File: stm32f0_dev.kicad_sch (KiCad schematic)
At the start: 38 parts, among them J1 USB_C_Receptacle_USB2.0, J2 left_bank, J3 SWD_header, J4 right_bank, SW1 SW_Push_Open_Dual, SW2 SW_SPDT, U2 AP2112K-3.3, U3 SN74LVC2G04DCKR, U4 CH340C, U5 MT29F2G01ABAGDWB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

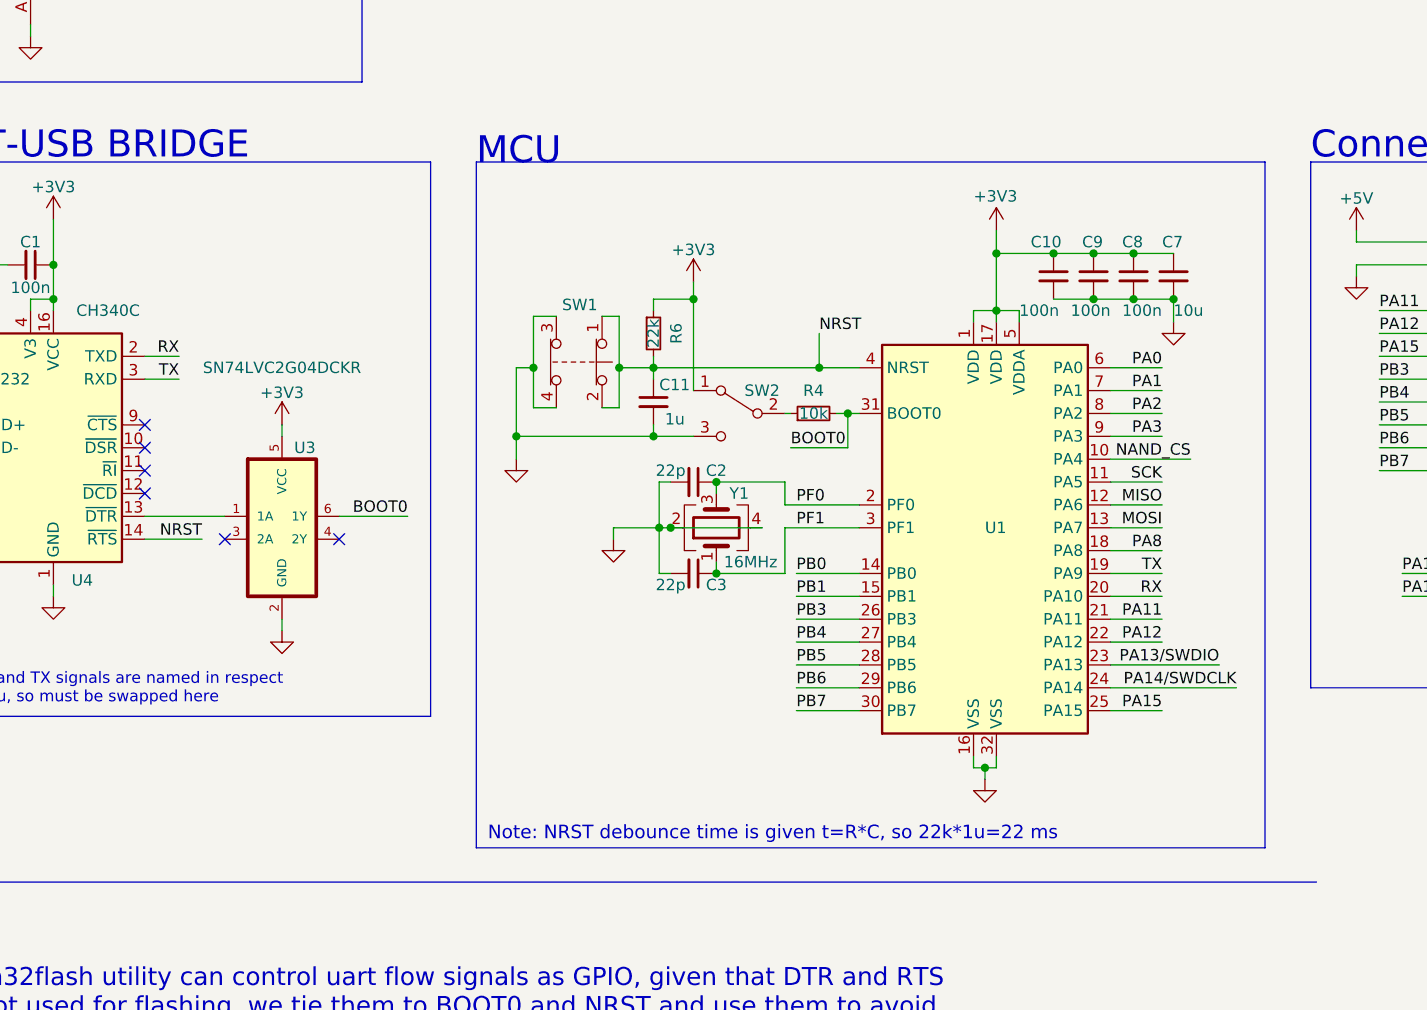
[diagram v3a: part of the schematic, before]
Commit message: Removed useless boot0 switch, uart IC is driving that signal
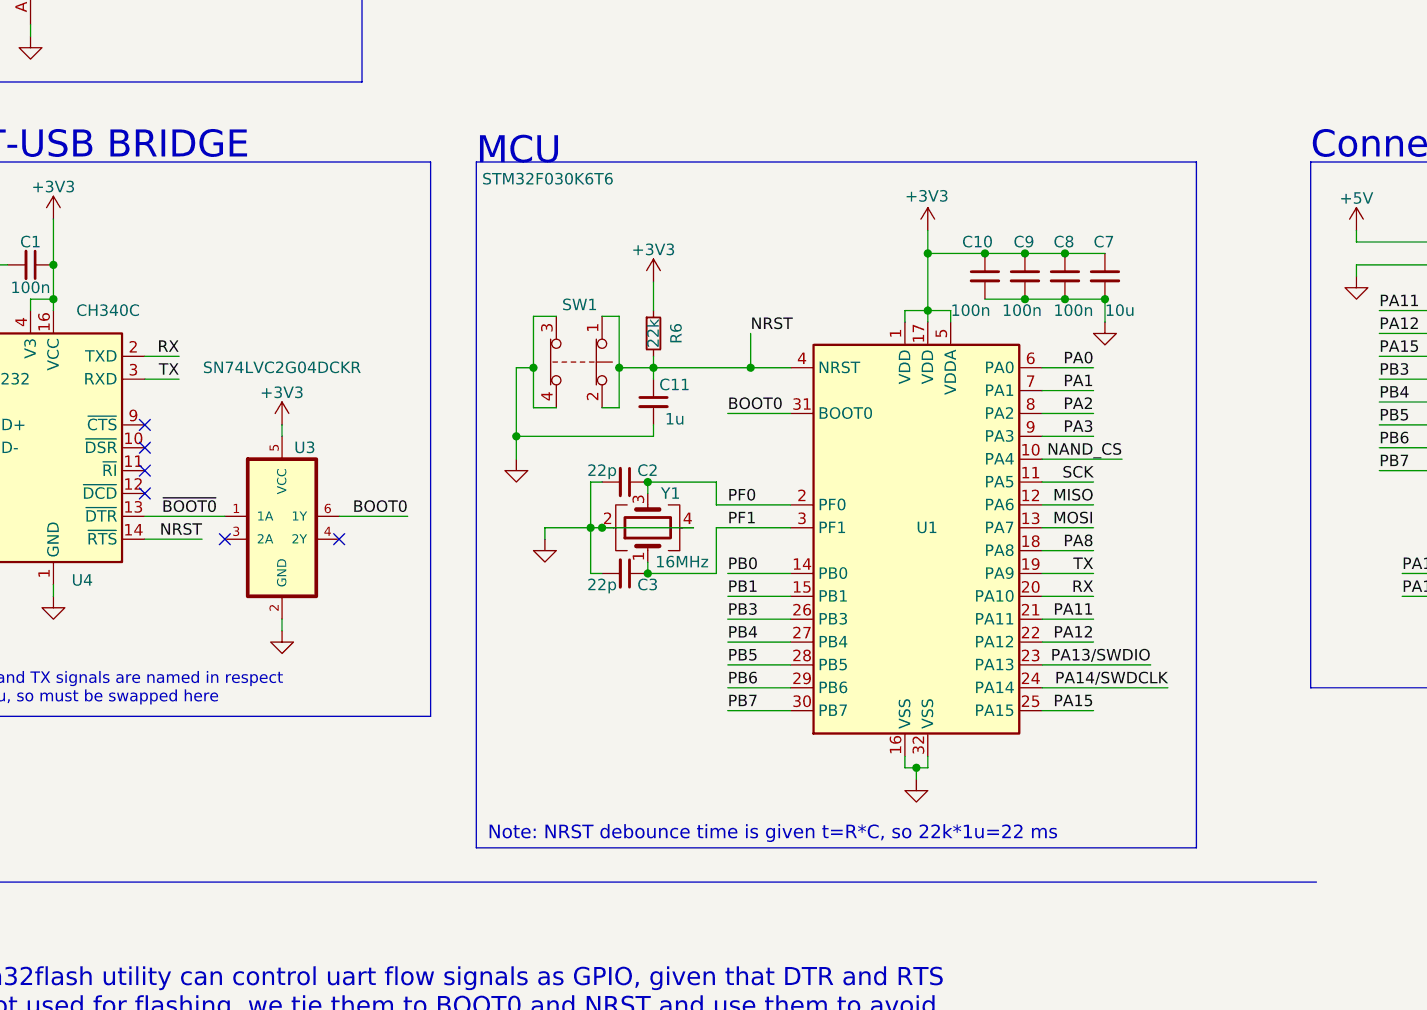
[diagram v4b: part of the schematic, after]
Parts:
- removed R4: 10k, Resistor_SMD:R_0603_1608Metric, symbol Device:R_Small
- removed SW2: SW_SPDT, SSSS811101 :SSSS811101, symbol Switch:SW_SPDT
- U1: value (none) -> STM32F030K6T6
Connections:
- net ~{BOOT0}: now reaches U3.1 (1A), U4.13 (~{DTR})
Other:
- moved on the sheet: C10, C2, C3, C7, C8, C9, U1, Y1
